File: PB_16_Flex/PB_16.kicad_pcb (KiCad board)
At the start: 2 copper layers, 162.6 x 50.8 mm, 33 parts, among them J1 USB, J2 OLED Conn, J3 GPIO Header, J4 RTC Conn, J5 Output 1, J6 Output 2, J7 DMX1, J8 DMX2, J9 Power Select, SW1 OLED Select, SW2 Enter BTN, SW3 Down BTN, U1 POCKETBEAGLE-SC-569, U2 UA9638CP, U3 24LC256

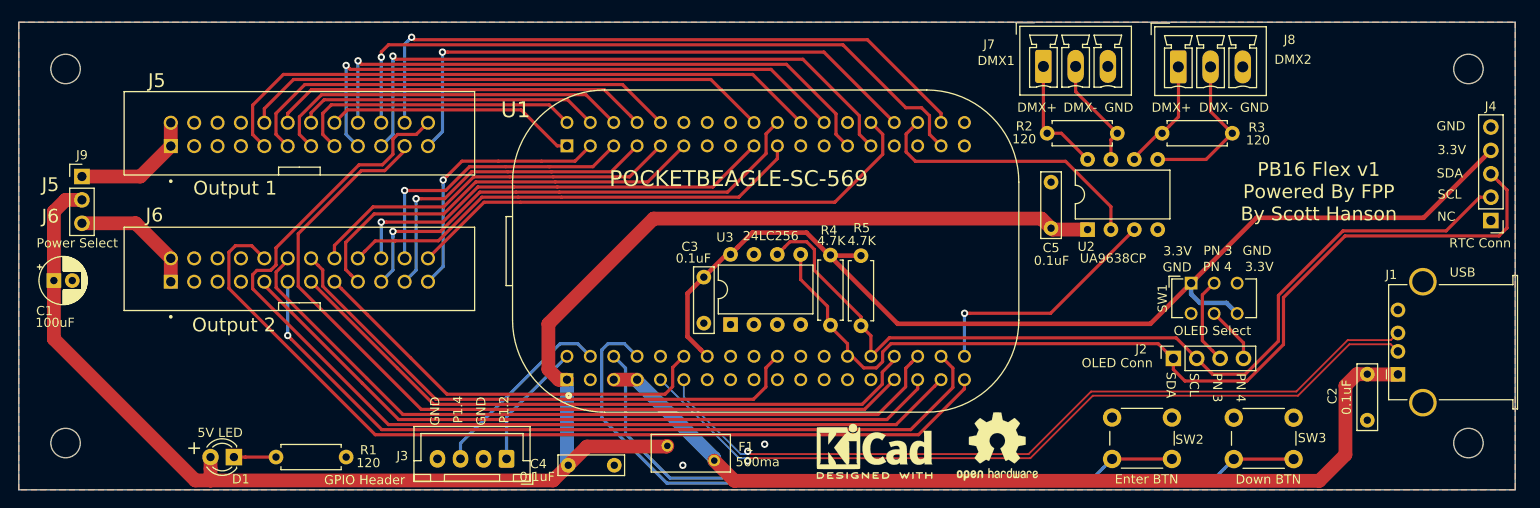
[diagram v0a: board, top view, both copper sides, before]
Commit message: fix hole spacing
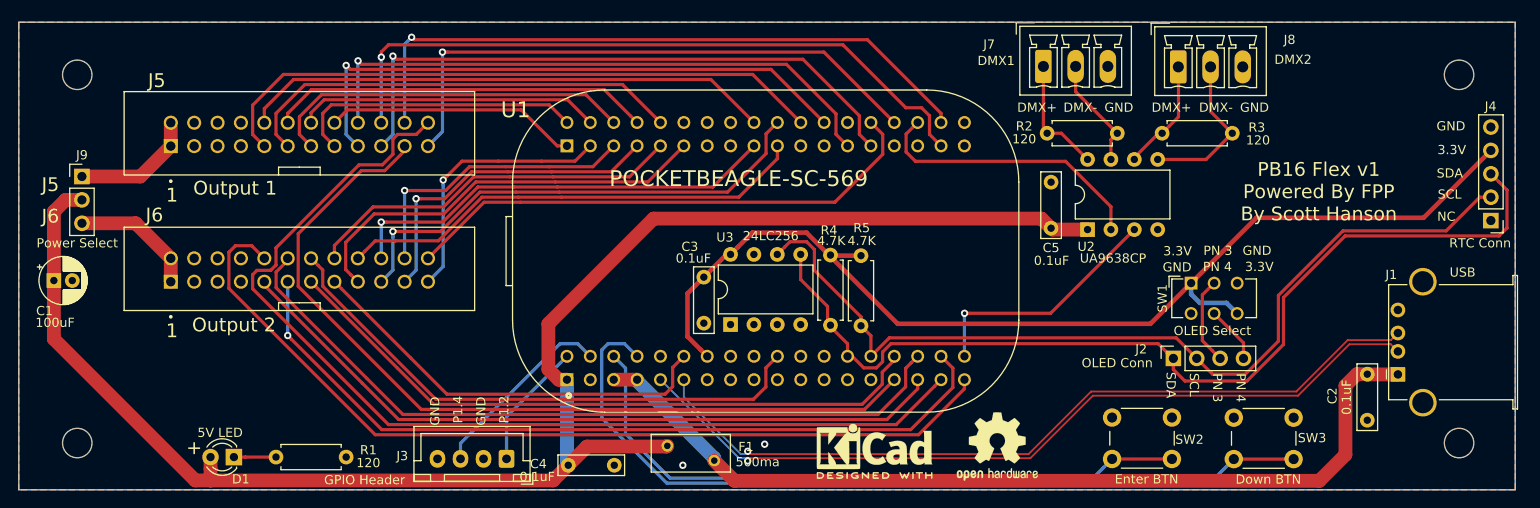
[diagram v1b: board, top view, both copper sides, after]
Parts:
- moved REF** 1.42 mm to (92.7, 76.8)
- moved REF** 1.27 mm to (92.7, 116.8)
- moved REF** 1.20 mm to (242.8, 76.8)
- moved REF** 1.02 mm to (242.8, 116.8)
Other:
- board text added: "1"
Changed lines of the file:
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@@
   (general
     (thickness 1.6)
-    (drawings 37)
+    (drawings 39)
     (tracks 457)
     (zones 0)
@@
     (mod_text_size 1 1)
     (mod_text_width 0.15)
-    (pad_size 1.524 1.524)
-    (pad_drill 0.762)
+    (pad_size 3.200001 3.200001)
+    (pad_drill 3.200001)
     (pad_to_mask_clearance 0.051)
     (solder_mask_min_width 0.25)
@@
   )
   (module MountingHole:MountingHole_3.2mm_M3 (layer F.Cu)
-    (at 243.84 76.2)
+    (at 242.824 76.835)
     (descr "Mounting Hole 3.2mm, no annular, M3")
     (tags "mounting hole 3.2mm no annular m3")
@@
   )
   (module MountingHole:MountingHole_3.2mm_M3 (layer F.Cu)
-    (at 91.44 76.2)
+    (at 92.71 76.835)
     (descr "Mounting Hole 3.2mm, no annular, M3")
     (tags "mounting hole 3.2mm no annular m3")
@@
   )
   (module MountingHole:MountingHole_3.2mm_M3 (layer F.Cu)
-    (at 243.84 116.84)
+    (at 242.824 116.84)
     (descr "Mounting Hole 3.2mm, no annular, M3")
     (tags "mounting hole 3.2mm no annular m3")
@@
   )
   (module MountingHole:MountingHole_3.2mm_M3 (layer F.Cu)
-    (at 91.44 116.84)
+    (at 92.71 116.84)
     (descr "Mounting Hole 3.2mm, no annular, M3")
     (tags "mounting hole 3.2mm no annular m3")
@@
     )
   )
+  (gr_text 1 (at 102.997 89.916) (layer F.SilkS)
+    (effects (font (size 1.5 1.5) (thickness 0.3)))
+  )
+  (gr_text 1 (at 102.997 104.648) (layer F.SilkS)
+    (effects (font (size 1.5 1.5) (thickness 0.3)))
+  )
   (gr_text J6 (at 89.789 92.202) (layer F.SilkS)
     (effects (font (size 1.5 1.5) (thickness 0.3)))
@@
   (segment (start 93.218 90.424) (end 91.44 90.424) (width 1.5) (layer F.Cu) (net 3))
   (segment (start 91.44 90.424) (end 90.17 91.694) (width 1.5) (layer F.Cu) (net 3))
-  (segment (start 110.978 118.364) (end 114.3 118.364) (width 0.35) (layer F.Cu) (net 64))
-  (segment (start 109.728 118.364) (end 110.978 118.364) (width 0.35) (layer F.Cu) (net 64))
   (segment (start 165.2445 118.0374) (end 165.5445 117.7374) (width 0.2) (layer B.Cu) (net 4))
   (segment (start 164.784957 118.0374) (end 165.2445 118.0374) (width 0.2) (layer B.Cu) (net 4))
@@
   (segment (start 218.186 83.185) (end 215.82368 80.82268) (width 0.35) (layer F.Cu) (net 33))
   (segment (start 210.0834 86.0298) (end 215.3412 86.0298) (width 0.35) (layer F.Cu) (net 33))
-  (segment (start 189.23 85.09) (end 188.526001 84.386001) (width 0.35) (layer F.Cu) (net 66))
   (segment (start 182.753 83.27136) (end 182.753 85.217) (width 0.35) (layer F.Cu) (net 34))
   (segment (start 184.00776 82.0166) (end 182.753 83.27136) (width 0.35) (layer F.Cu) (net 34))
@@
   (segment (start 99.06 92.964) (end 102.87 96.774) (width 1.5) (layer F.Cu) (net 63))
   (segment (start 93.218 92.964) (end 99.06 92.964) (width 1.5) (layer F.Cu) (net 63))
+  (segment (start 110.978 118.364) (end 114.3 118.364) (width 0.35) (layer F.Cu) (net 64))
+  (segment (start 109.728 118.364) (end 110.978 118.364) (width 0.35) (layer F.Cu) (net 64))
+  (segment (start 189.23 85.09) (end 188.526001 84.386001) (width 0.35) (layer F.Cu) (net 66))
   (zone (net 1) (net_name GND) (layer F.Cu) (hatch edge 0.508)
     (connect_pads (clearance 0.28))

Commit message: moved OLED
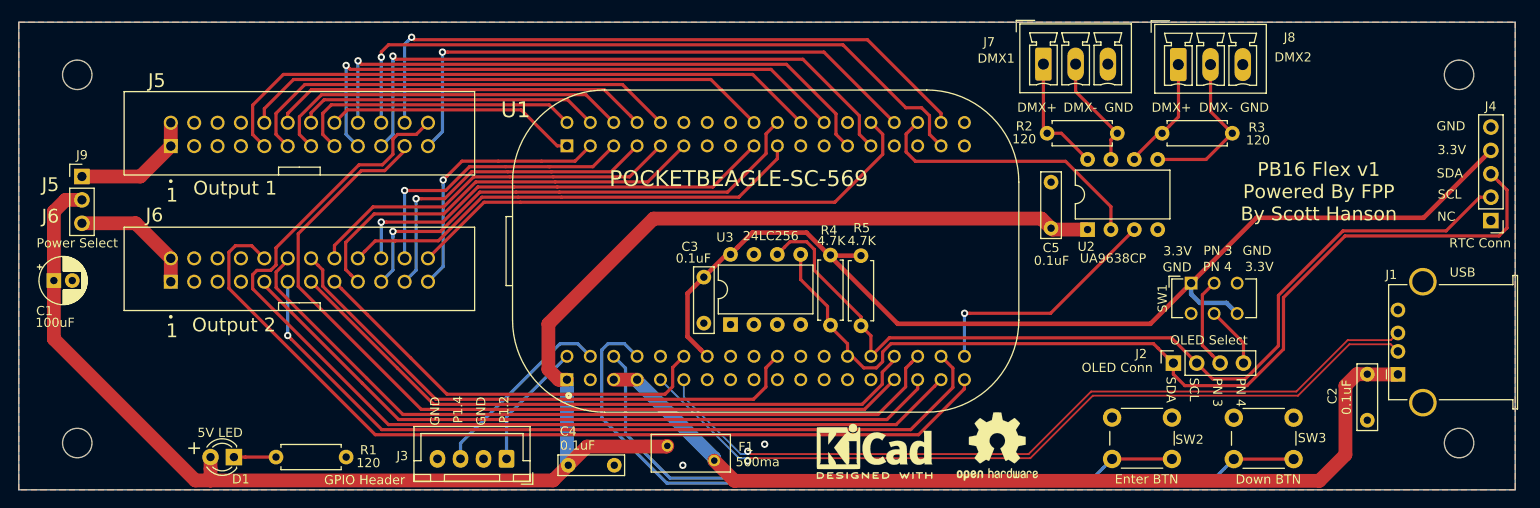
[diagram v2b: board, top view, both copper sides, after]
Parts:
- moved J2 0.51 mm to (211.8, 108.2)
- moved J7 0.25 mm to (197.7, 75.7)
- moved J8 0.25 mm to (212.3, 75.7)
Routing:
- net I2C_SDA: track 105.9 -> 106.6 mm
- net I2C_SCL: track 99.8 -> 100.5 mm
- net /Serial/DMX1+: track 13.6 -> 13.0 mm
- net /OLED_Pin_3: track 9.51 -> 10.0 mm
- net /OLED_Pin_4: track 6.20 -> 6.71 mm
- net /Serial/DMX2+: track 12.3 -> 12.8 mm
- net /Serial/DMX2-: track 18.4 -> 18.9 mm

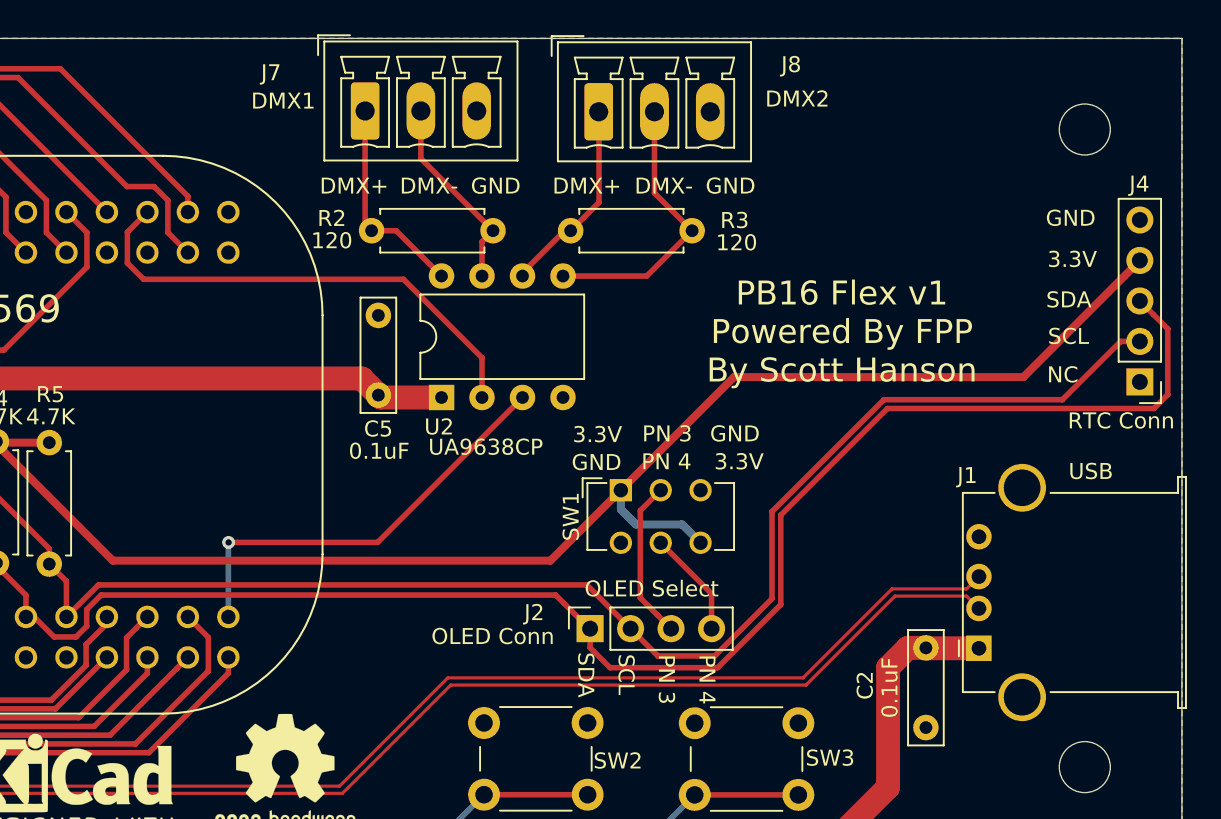
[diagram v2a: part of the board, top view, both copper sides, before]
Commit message: added more space for OLED
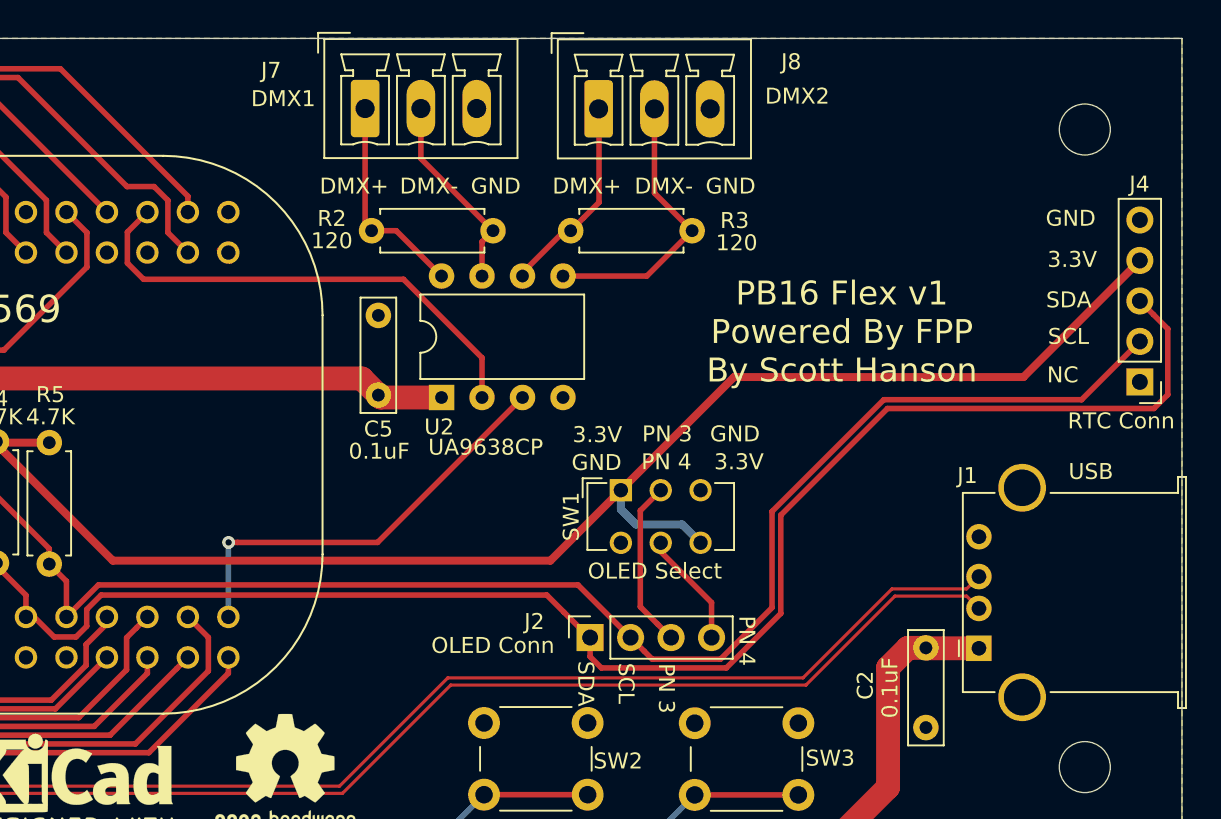
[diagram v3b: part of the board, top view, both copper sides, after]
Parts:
- moved J2 0.56 mm to (211.8, 108.7)
- moved J8 0.18 mm to (212.3, 75.5)
- moved J7 0.15 mm to (197.7, 75.5)
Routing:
- net /OLED_Pin_4: track 6.71 -> 7.27 mm
- net /OLED_Pin_3: track 10.0 -> 10.6 mm

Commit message: added BBB16 Flex
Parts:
- removed C2: 0.1uF, Capacitor_THT:C_Rect_L7.0mm_W2.0mm_P5.00mm
- removed F1: 500ma, Fuse:Fuse_BelFuse_0ZRE0005FF_L8.3mm_W3.8mm
- added C6: 0.1uF, Capacitor_SMD:C_0805_2012Metric_Pad1.15x1.40mm_HandSolder, F.Cu at (229.8, 110.2)
- added FB1: 150 OHM, Inductor_SMD:L_0805_2012Metric_Pad1.15x1.40mm_HandSolder, F.Cu at (232.8, 109.2)
- added R6: 10K, Resistor_SMD:R_0805_2012Metric_Pad1.15x1.40mm_HandSolder, F.Cu at (149.5, 117.6)
- added R7: 10K, Resistor_SMD:R_0805_2012Metric_Pad1.15x1.40mm_HandSolder, F.Cu at (149.5, 115.2)
- added U4: TPS2051BDBVR, digikey-footprints:SOT-753, F.Cu at (153.8, 116.6)
- added U5: TPD4S009DBVR, Package_TO_SOT_SMD:SOT-23-6_Handsoldering, F.Cu at (231.7, 105.7)
- C1: footprint Capacitor_THT:CP_Radial_D5.0mm_P2.00mm -> Capacitor_SMD:CP_Elec_6.3x5.4_Nichicon
- C3, C4, C5: footprint Capacitor_THT:C_Rect_L7.0mm_W2.0mm_P5.00mm -> Capacitor_SMD:C_0805_2012Metric_Pad1.15x1.40mm_HandSolder
- D1: footprint LED_THT:LED_D3.0mm -> LED_SMD:LED_0805_2012Metric_Pad1.15x1.40mm_HandSolder
- R1: value 120 -> 1K; footprint Resistor_THT:R_Axial_DIN0207_L6.3mm_D2.5mm_P7.62mm_Horizontal -> Resistor_SMD:R_0805_2012Metric_Pad1.15x1.40mm_HandSolder
- R2, R3, R4, R5: footprint Resistor_THT:R_Axial_DIN0207_L6.3mm_D2.5mm_P7.62mm_Horizontal -> Resistor_SMD:R_0805_2012Metric_Pad1.15x1.40mm_HandSolder
- U2, U3: footprint Package_DIP:DIP-8_W7.62mm -> Package_SO:SOIC-8_3.9x4.9mm_P1.27mm
- moved C3 14.7 mm to (167.3, 90.6)
- moved U3 14.1 mm to (171.1, 92.0)
- moved R1 9.37 mm to (112.5, 118.4)
- moved R4 7.74 mm to (176.7, 89.0)
- moved R5 7.56 mm to (178.9, 89.0)
- moved U2 6.88 mm to (205.3, 87.4)
- moved C5 5.54 mm to (201.5, 88.8)
- moved C1 4.69 mm to (92.7, 103.1)
- moved R3 3.91 mm to (214.0, 81.4)
- moved C4 3.37 mm to (143.7, 116.9), turned to 90 degrees
- moved R2 2.36 mm to (199.6, 81.4)
- moved U1 1.93 mm to (167.5, 94.1)
- moved D1 1.50 mm to (108.2, 118.4)
- moved J1 0.41 mm to (236.6, 109.2)
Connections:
- C3 pad 2: +3V3 -> +3.3VP
- C5 pad 1: +5V -> 5V_Serial
- J1 pad 1: V_USB -> /USB/VBUS
- R4 pad 1: +3V3 -> +3.3VP
- R5 pad 1: +3V3 -> +3.3VP
- U1 pad P1_24: Net-(U1-PadP1_24) -> 5V_Serial
- U1 pad P1_3: Net-(U1-PadP1_3) -> USB_DVBUS
- U1 pad P2_23: Net-(U1-PadP2_23) -> +3.3VP
- U2 pad 1: +5V -> 5V_Serial
- U3 pad 8: +3V3 -> +3.3VP
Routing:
- net +5V: track 175.1 -> 107.7 mm
- net OUT16: track 112.4 -> 71.4 mm, vias 0 -> 2
- net 5V_Serial: track 0.00 -> 39.6 mm, vias 0 -> 1
- net OUT13: track 93.1 -> 66.1 mm, vias 0 -> 2
- net +3.3VP: track 0.00 -> 20.0 mm, vias 0 -> 1
- net OUT19: track 88.2 -> 75.2 mm
- net USB_DVBUS: track 0.00 -> 12.8 mm
- net OUT18: track 98.2 -> 86.1 mm
- net BTN2: track 91.3 -> 81.7 mm
- net +3V3: track 120.0 -> 127.7 mm
- net I2C_SCL: track 101.0 -> 108.1 mm, vias 0 -> 2
- net OUT20: track 82.9 -> 77.2 mm, vias 0 -> 1
- net USB_D+: track 87.7 -> 91.8 mm, vias 1 -> 0
- net USB_D-: track 89.3 -> 93.2 mm, vias 1 -> 0
- net GPIO2: track 20.8 -> 24.0 mm
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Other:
- net class usb added: clearance 0.2, trace_width 0.35, via_dia 0.8, via_drill 0.4
- board text added: "PB16 Flex v1.1 Powered By FPP By Scott Hanson"
- board text removed: "PB16 Flex v1 Powered By FPP By Scott Hanson"

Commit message: added v6 PCB
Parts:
- added G***: LOGO, Scotts:chewi_10, F.Cu at (213.5, 88.6)
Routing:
- net GND: vias 108 -> 120
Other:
- net class 3.3v removed
- net class 5v removed
- net class Default removed
- net class Gnd removed
- net class Power removed
- net class Vin removed
- net class power2 removed
- net class usb removed

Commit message: fix warnings
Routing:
- net /Serial/DMX2-: track 16.6 -> 15.5 mm
- net GPIO1: track 16.7 -> 15.8 mm
- net OUT18: track 86.1 -> 85.4 mm
- net /OLED_Pin_4: track 8.00 -> 7.44 mm

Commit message: untested
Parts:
- removed REF**: OSHW-Logo2_9.8x8mm_SilkScreen, Symbol:OSHW-Logo2_9.8x8mm_SilkScreen
- removed REF**: KiCad-Logo2_5mm_SilkScreen, Symbol:KiCad-Logo2_5mm_SilkScreen
- removed SW1: OLED Select, Button_Switch_THT:SW_CuK_JS202011CQN_DPDT_Straight
- added JP1: PIN_3_JMP, Scotts:SolderJumper-3_P1mm_Bridged12, B.Cu at (215.7, 99.8)
- added JP2: PIN_4_JMP, Scotts:SolderJumper-3_P1mm_Bridged23, B.Cu at (218.5, 99.8)
- C3, C4, C5, C6: footprint Capacitor_SMD:C_0805_2012Metric_Pad1.15x1.40mm_HandSolder -> Capacitor_SMD:C_0805_2012Metric
- H1, H2, H3, H4: renamed from REF**; value MountingHole_3.2mm_M3 -> MountingHole; footprint MountingHole:MountingHole_3.2mm_M3 -> Scotts:MountingHole_3.7mm
- R1, R2, R3, R4, R5, R6, R7: footprint Resistor_SMD:R_0805_2012Metric_Pad1.15x1.40mm_HandSolder -> Resistor_SMD:R_0805_2012Metric
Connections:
- J4 pad 1: Net-(J4-Pad1) -> unconnected-(J4-Pin_1-Pad1)
- J5 pad 3: Net-(J5-Pad3) -> unconnected-(J5-Pin_3-Pad3)
- J5 pad 4: Net-(J5-Pad4) -> unconnected-(J5-Pin_4-Pad4)
- J5 pad 5: Net-(J5-Pad5) -> unconnected-(J5-Pin_5-Pad5)
- J5 pad 6: Net-(J5-Pad6) -> unconnected-(J5-Pin_6-Pad6)
- J6 pad 3: Net-(J6-Pad3) -> unconnected-(J6-Pin_3-Pad3)
- J6 pad 4: Net-(J6-Pad4) -> unconnected-(J6-Pin_4-Pad4)
- J6 pad 5: Net-(J6-Pad5) -> unconnected-(J6-Pin_5-Pad5)
- J6 pad 6: Net-(J6-Pad6) -> unconnected-(J6-Pin_6-Pad6)
- U1 pad P1_10: Net-(U1-PadP1_10) -> unconnected-(U1A-SPI0_MISO-PadP1_10)
- U1 pad P1_18: Net-(U1-PadP1_18) -> unconnected-(U1A-AIN1.8V_REF+-PadP1_18)
- U1 pad P1_19: Net-(U1-PadP1_19) -> unconnected-(U1A-AIN0(1.8V)-PadP1_19)
- U1 pad P1_21: Net-(U1-PadP1_21) -> unconnected-(U1A-AIN1(1.8V)-PadP1_21)
- U1 pad P1_23: Net-(U1-PadP1_23) -> unconnected-(U1A-AIN2(1.8V)-PadP1_23)
- U1 pad P1_25: Net-(U1-PadP1_25) -> unconnected-(U1A-AIN3(1.8V)-PadP1_25)
- U1 pad P1_27: Net-(U1-PadP1_27) -> unconnected-(U1A-AIN4(1.8V)-PadP1_27)
- U1 pad P2_12: Net-(U1-PadP2_12) -> unconnected-(U1B-SYS_PWRBTN-PadP2_12)
- U1 pad P2_13: Net-(U1-PadP2_13) -> unconnected-(U1A-SYS_VOUT-PadP2_13)
- U1 pad P2_14: Net-(U1-PadP2_14) -> unconnected-(U1B-BAT_VIN-PadP2_14)
- U1 pad P2_16: Net-(U1-PadP2_16) -> unconnected-(U1B-BAT_TEMP-PadP2_16)
- U1 pad P2_26: Net-(U1-PadP2_26) -> unconnected-(U1B-SYS_NRST-PadP2_26)
- U1 pad P2_29: Net-(U1-PadP2_29) -> unconnected-(U1B-SPI1_CLK-PadP2_29)
- U1 pad P2_31: Net-(U1-PadP2_31) -> unconnected-(U1B-SPI1_CS-PadP2_31)
- U1 pad P2_35: Net-(U1-PadP2_35) -> unconnected-(U1B-AIN5/GPIO86-PadP2_35)
- U1 pad P2_36: Net-(U1-PadP2_36) -> unconnected-(U1B-AIN7(1.8V)-PadP2_36)
- U5 pad 1: Net-(U5-Pad1) -> unconnected-(U5-D1+-Pad1)
- U5 pad 6: Net-(U5-Pad6) -> unconnected-(U5-D1--Pad6)
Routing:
- net /OLED_Pin_4: track 7.44 -> 10.4 mm
- net /OLED_Pin_3: track 10.5 -> 11.2 mm
- net +3V3: track 127.7 -> 127.5 mm, vias 0 -> 1
- net GND: vias 120 -> 123
